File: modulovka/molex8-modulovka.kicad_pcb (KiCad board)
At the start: 2 copper layers, 42 x 42 mm, 7 parts, among them J1 2xMVE252-5-V, J2 TME 39281083 MOLEX, J3 2xMVE252-5-V

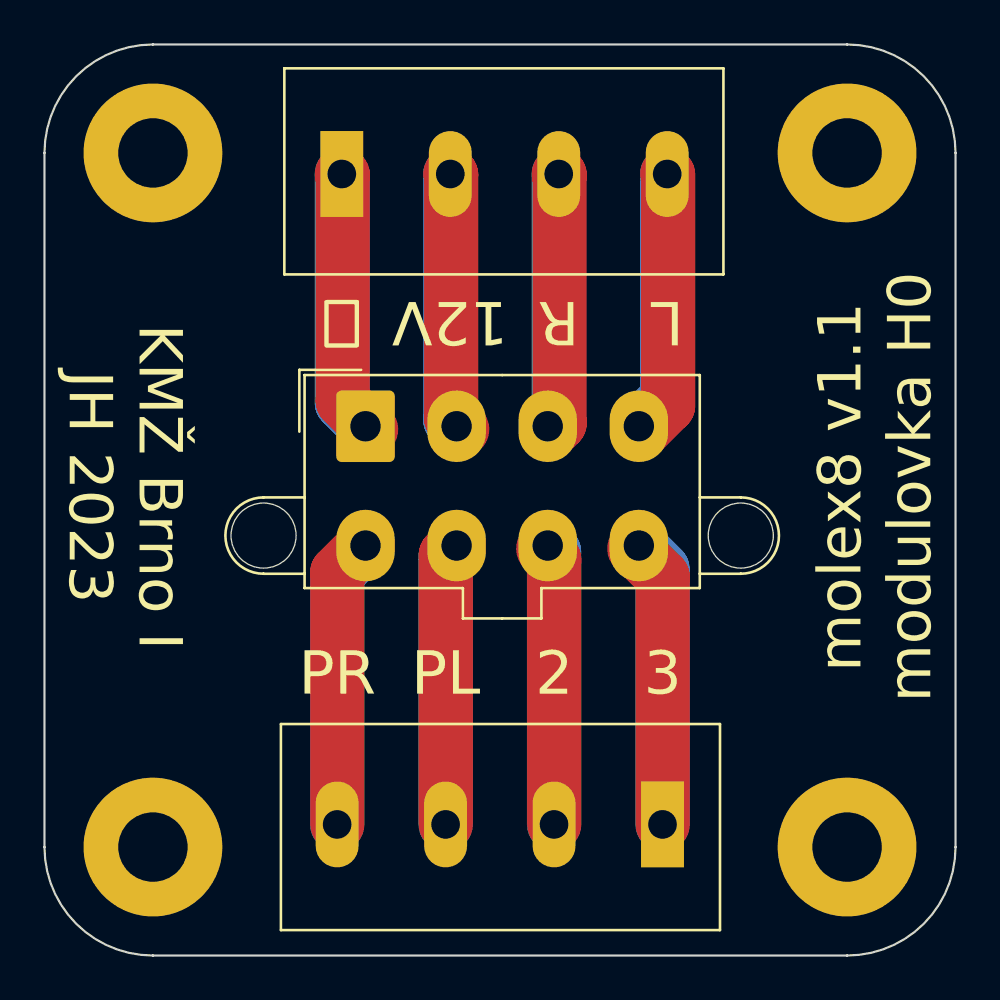
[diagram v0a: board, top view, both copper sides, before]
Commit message: modulovka: name wires, fix conn symbol, fix switched 2-3.
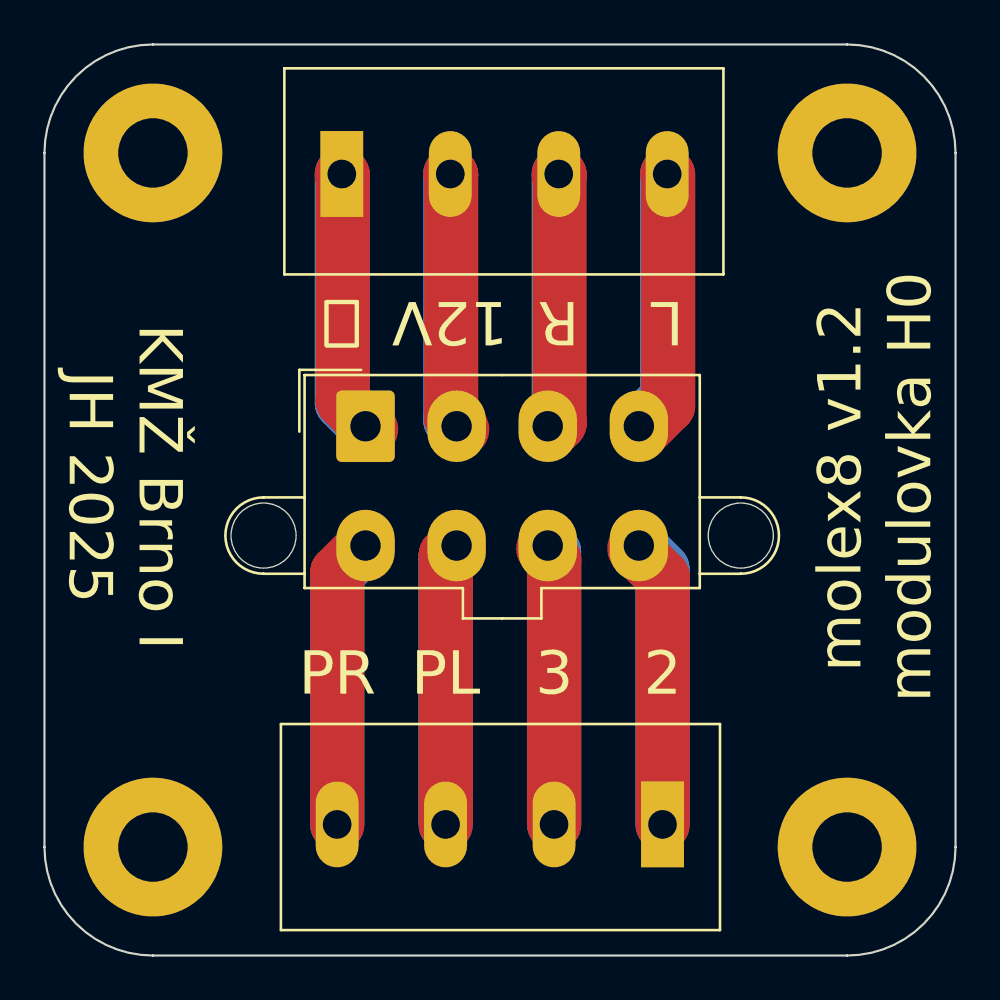
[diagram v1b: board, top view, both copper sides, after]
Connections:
- net Net-(J1-Pin_1) renamed /GND
- net Net-(J1-Pin_2) renamed /12V
- net Net-(J1-Pin_3) renamed /R
- net Net-(J1-Pin_4) renamed /L
- net Net-(J2-Pin_5) renamed /PR
- net Net-(J2-Pin_6) renamed /PL
- net Net-(J2-Pin_7) renamed /3
- net Net-(J2-Pin_8) renamed /2
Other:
- board text added: "KMŽ Brno I JH 2025"
- board text added: "molex8 v1.2 modulovka H0"
- board text removed: "KMŽ Brno I JH 2023"
- board text removed: "molex8 v1.1 modulovka H0"
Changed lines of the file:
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@@
 	)
 	(net 0 "")
-	(net 1 "Net-(J1-Pin_1)")
-	(net 2 "Net-(J1-Pin_2)")
-	(net 3 "Net-(J1-Pin_3)")
-	(net 4 "Net-(J1-Pin_4)")
-	(net 5 "Net-(J2-Pin_5)")
-	(net 6 "Net-(J2-Pin_6)")
-	(net 7 "Net-(J2-Pin_7)")
-	(net 8 "Net-(J2-Pin_8)")
+	(net 1 "/L")
+	(net 2 "/GND")
+	(net 3 "/R")
+	(net 4 "/12V")
+	(net 5 "/PR")
+	(net 6 "/PL")
+	(net 7 "/2")
+	(net 8 "/3")
 	(footprint "Connector_Molex:Molex_Mini-Fit_Jr_5566-08A2_2x04_P4.20mm_Vertical"
 		(layer "F.Cu")
@@
 			)
 		)
-		(property "Description" "Generic connector, double row, 02x04, counter clockwise pin numbering scheme (similar to DIP package numbering), script generated (kicad-library-utils/schlib/autogen/connector/)"
+		(property "Description" "Generic connector, double row, 02x04, top/bottom pin numbering scheme (row 1: 1...pins_per_row, row2: pins_per_row+1 ... num_pins), script generated (kicad-library-utils/schlib/autogen/connector/)"
 			(at 0 0 0)
 			(layer "F.Fab")
@@
 			)
 		)
+		(property ki_fp_filters "Connector*:*_2x??_*")
+		(sheetname "/")
 		(sheetfile "molex8-modulovka.kicad_sch")
 		(attr through_hole)
@@
 			(remove_unused_layers no)
 			(roundrect_rratio 0.092593)
-			(net 1 "Net-(J1-Pin_1)")
+			(net 2 "/GND")
 			(pinfunction "Pin_1")
 			(pintype "passive")
@@
 			(layers "*.Cu" "*.Mask")
 			(remove_unused_layers no)
-			(net 2 "Net-(J1-Pin_2)")
+			(net 4 "/12V")
 			(pinfunction "Pin_2")
 			(pintype "passive")
@@
 			(layers "*.Cu" "*.Mask")
 			(remove_unused_layers no)
-			(net 3 "Net-(J1-Pin_3)")
+			(net 3 "/R")
 			(pinfunction "Pin_3")
 			(pintype "passive")
@@
 			(layers "*.Cu" "*.Mask")
 			(remove_unused_layers no)
-			(net 4 "Net-(J1-Pin_4)")
+			(net 1 "/L")
 			(pinfunction "Pin_4")
 			(pintype "passive")
@@
 			(layers "*.Cu" "*.Mask")
 			(remove_unused_layers no)
-			(net 5 "Net-(J2-Pin_5)")
+			(net 5 "/PR")
 			(pinfunction "Pin_5")
 			(pintype "passive")
@@
 			(layers "*.Cu" "*.Mask")
 			(remove_unused_layers no)
-			(net 6 "Net-(J2-Pin_6)")
+			(net 6 "/PL")
 			(pinfunction "Pin_6")
 			(pintype "passive")
@@
 			(layers "*.Cu" "*.Mask")
 			(remove_unused_layers no)
-			(net 7 "Net-(J2-Pin_7)")
+			(net 8 "/3")
 			(pinfunction "Pin_7")
 			(pintype "passive")
@@
 			(layers "*.Cu" "*.Mask")
 			(remove_unused_layers no)
-			(net 8 "Net-(J2-Pin_8)")
+			(net 7 "/2")
 			(pinfunction "Pin_8")
 			(pintype "passive")
@@
 			)
 		)
-		(property "Description" "Mounting Hole without connection"
+		(property "Description" ""
 			(at 0 0 0)
 			(layer "F.Fab")
@@
 			)
 		)
+		(property ki_fp_filters "MountingHole*")
+		(sheetname "/")
 		(sheetfile "molex8-modulovka.kicad_sch")
 		(attr exclude_from_pos_files)
@@
 			)
 		)
-		(property "Description" "Generic screw terminal, single row, 01x04, script generated (kicad-library-utils/schlib/autogen/connector/)"
+		(property "Description" ""
 			(at 0 0 0)
 			(layer "F.Fab")
@@
 			)
 		)
+		(property ki_fp_filters "TerminalBlock*:*")
+		(sheetname "/")
 		(sheetfile "molex8-modulovka.kicad_sch")
 		(attr through_hole)
@@
 			(layers "*.Cu" "*.Mask")
 			(remove_unused_layers no)
-			(net 1 "Net-(J1-Pin_1)")
+			(net 2 "/GND")
 			(pinfunction "Pin_1")
 			(pintype "passive")
@@
 			(layers "*.Cu" "*.Mask")
 			(remove_unused_layers no)
-			(net 2 "Net-(J1-Pin_2)")
+			(net 4 "/12V")
 			(pinfunction "Pin_2")
 			(pintype "passive")
@@
 			(layers "*.Cu" "*.Mask")
 			(remove_unused_layers no)
-			(net 3 "Net-(J1-Pin_3)")
+			(net 3 "/R")
 			(pinfunction "Pin_3")
 			(pintype "passive")
@@
 			(layers "*.Cu" "*.Mask")
 			(remove_unused_layers no)
-			(net 4 "Net-(J1-Pin_4)")
+			(net 1 "/L")
 			(pinfunction "Pin_4")
 			(pintype "passive")
@@
 			)
 		)
-		(property "Description" "Generic screw terminal, single row, 01x04, script generated (kicad-library-utils/schlib/autogen/connector/)"
+		(property "Description" ""
 			(at 0 0 180)
 			(layer "F.Fab")
@@
 			)
 		)
+		(property ki_fp_filters "TerminalBlock*:*")
+		(sheetname "/")
 		(sheetfile "molex8-modulovka.kicad_sch")
 		(attr through_hole)
@@
 			(layers "*.Cu" "*.Mask")
 			(remove_unused_layers no)
-			(net 8 "Net-(J2-Pin_8)")
+			(net 7 "/2")
 			(pinfunction "Pin_1")
 			(pintype "passive")
@@
 			(layers "*.Cu" "*.Mask")
 			(remove_unused_layers no)
-			(net 7 "Net-(J2-Pin_7)")
+			(net 8 "/3")
 			(pinfunction "Pin_2")
 			(pintype "passive")
@@
 			(layers "*.Cu" "*.Mask")
 			(remove_unused_layers no)
-			(net 6 "Net-(J2-Pin_6)")
+			(net 6 "/PL")
 			(pinfunction "Pin_3")
 			(pintype "passive")
@@
 			(layers "*.Cu" "*.Mask")
 			(remove_unused_layers no)
-			(net 5 "Net-(J2-Pin_5)")
+			(net 5 "/PR")
 			(pinfunction "Pin_4")
 			(pintype "passive")
@@
 			)
 		)
-		(property "Description" "Mounting Hole without connection"
+		(property "Description" ""
 			(at 0 0 0)
 			(layer "F.Fab")
@@
 			)
 		)
+		(property ki_fp_filters "MountingHole*")
+		(sheetname "/")
 		(sheetfile "molex8-modulovka.kicad_sch")
 		(attr exclude_from_pos_files)
@@
 			)
 		)
-		(property "Description" "Mounting Hole without connection"
+		(property "Description" ""
 			(at 0 0 0)
 			(layer "F.Fab")
@@
 			)
 		)
+		(property ki_fp_filters "MountingHole*")
+		(sheetname "/")
 		(sheetfile "molex8-modulovka.kicad_sch")
 		(attr exclude_from_pos_files)
@@
 			)
 		)
-		(property "Description" "Mounting Hole without connection"
+		(property "Description" ""
 			(at 0 0 0)
 			(layer "F.Fab")
@@
 			)
 		)
+		(property ki_fp_filters "MountingHole*")
+		(sheetname "/")
 		(sheetfile "molex8-modulovka.kicad_sch")
 		(attr exclude_from_pos_files)
@@
 		)
 	)
-	(gr_text "3"
+	(gr_text "2"
 		(at 109 103 0)
 		(layer "F.SilkS")
@@
 		)
 	)
-	(gr_text "molex8 v1.1\nmodulovka H0"
+	(gr_text "molex8 v1.2\nmodulovka H0"
 		(at 118.8 94.4 90)
 		(layer "F.SilkS")
@@
 		)
 	)
-	(gr_text "KMŽ Brno I\nJH 2023"
+	(gr_text "KMŽ Brno I\nJH 2025"
 		(at 84.2 94.4 270)
 		(layer "F.SilkS")
@@
 		)
 	)
-	(gr_text "2"
+	(gr_text "3"
 		(at 104 103 0)
 		(layer "F.SilkS")
@@
 	)
 	(segment
-		(start 94.25 90.435)
-		(end 94.25 80.014)
+		(start 109.25 80.014)
+		(end 109.208 79.972)
 		(width 2.5)
 		(layer "F.Cu")
@@
 	)
 	(segment
-		(start 94.25 80.014)
-		(end 94.208 79.972)
+		(start 108.158 91.743)
+		(end 109.25 90.651)
 		(width 2.5)
 		(layer "F.Cu")
@@
 	)
 	(segment
-		(start 95.558 91.743)
-		(end 94.25 90.435)
+		(start 109.25 90.651)
+		(end 109.25 80.014)
 		(width 2.5)
 		(layer "F.Cu")
@@
 	)
 	(segment
-		(start 94.208 90.508)
-		(end 95.3 91.6)
+		(start 109.208 90.292)
+		(end 107.9 91.6)
 		(width 2.5)
 		(layer "B.Cu")
@@
 	)
 	(segment
-		(start 94.208 79.972)
-		(end 94.208 90.508)
+		(start 109.208 79.972)
+		(end 109.208 90.292)
 		(width 2.5)
 		(layer "B.Cu")
@@
 	)
 	(segment
-		(start 99.758 91.743)
-		(end 99.25 91.235)
+		(start 94.25 90.435)
+		(end 94.25 80.014)
 		(width 2.5)
 		(layer "F.Cu")
@@
 	)
 	(segment
-		(start 99.25 91.235)
-		(end 99.25 80.014)
+		(start 94.25 80.014)
+		(end 94.208 79.972)
 		(width 2.5)
 		(layer "F.Cu")
@@
 	)
 	(segment
-		(start 99.25 80.014)
-		(end 99.208 79.972)
+		(start 95.558 91.743)
+		(end 94.25 90.435)
 		(width 2.5)
 		(layer "F.Cu")
@@
 	)
 	(segment
-		(start 99.208 91.308)
-		(end 99.5 91.6)
+		(start 94.208 90.508)
+		(end 95.3 91.6)
 		(width 2.5)
 		(layer "B.Cu")
@@
 	)
 	(segment
-		(start 99.208 79.972)
-		(end 99.208 91.308)
+		(start 94.208 79.972)
+		(end 94.208 90.508)
 		(width 2.5)
 		(layer "B.Cu")
@@
 	)
 	(segment
-		(start 109.25 80.014)
-		(end 109.208 79.972)
+		(start 99.758 91.743)
+		(end 99.25 91.235)
 		(width 2.5)
 		(layer "F.Cu")
@@
 	)
 	(segment
-		(start 108.158 91.743)
-		(end 109.25 90.651)
+		(start 99.25 91.235)
+		(end 99.25 80.014)
 		(width 2.5)
 		(layer "F.Cu")
@@
 	)
 	(segment
-		(start 109.25 90.651)
-		(end 109.25 80.014)
+		(start 99.25 80.014)
+		(end 99.208 79.972)
 		(width 2.5)
 		(layer "F.Cu")
@@
 	)
 	(segment
-		(start 109.208 90.292)
-		(end 107.9 91.6)
+		(start 99.208 91.308)
+		(end 99.5 91.6)
 		(width 2.5)
 		(layer "B.Cu")
@@
 	)
 	(segment
-		(start 109.208 79.972)
-		(end 109.208 90.292)
+		(start 99.208 79.972)
+		(end 99.208 91.308)
 		(width 2.5)
 		(layer "B.Cu")
@@
 	)
 	(segment
-		(start 104 97.749)
-		(end 103.492 97.241)
+		(start 109 109.951)
+		(end 109 98.549)
 		(width 2.5)
 		(layer "F.Cu")
@@
 	)
 	(segment
-		(start 104 109.951)
-		(end 104 97.749)
+		(start 109 98.549)
+		(end 107.692 97.241)
 		(width 2.5)
 		(layer "F.Cu")
@@
 	)
 	(segment
-		(start 103.992 97.392)
-		(end 103.7 97.1)
+		(start 108.992 98.192)
+		(end 107.9 97.1)
 		(width 2.5)
 		(layer "B.Cu")
@@
 	)
 	(segment
-		(start 103.992 109.956)
-		(end 103.992 97.392)
+		(start 108.992 109.956)
+		(end 108.992 98.192)
 		(width 2.5)
 		(layer "B.Cu")
@@
 	)
 	(segment
-		(start 109 109.951)
-		(end 109 98.549)
+		(start 104 97.749)
+		(end 103.492 97.241)
 		(width 2.5)
 		(layer "F.Cu")
@@
 	)
 	(segment
-		(start 109 98.549)
-		(end 107.692 97.241)
+		(start 104 109.951)
+		(end 104 97.749)
 		(width 2.5)
 		(layer "F.Cu")
@@
 	)
 	(segment
-		(start 108.992 98.192)
-		(end 107.9 97.1)
+		(start 103.992 97.392)
+		(end 103.7 97.1)
 		(width 2.5)
 		(layer "B.Cu")
@@
 	)
 	(segment
-		(start 108.992 109.956)
-		(end 108.992 98.192)
+		(start 103.992 109.956)
+		(end 103.992 97.392)
 		(width 2.5)
 		(layer "B.Cu")
